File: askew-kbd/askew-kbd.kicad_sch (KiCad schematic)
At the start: 45 parts, among them SW1 SW_PUSH, SW10 SW_PUSH, SW11 SW_PUSH, SW12 SW_PUSH, SW13 SW_PUSH, SW14 SW_PUSH, SW15 SW_PUSH, SW16 SW_PUSH, SW17 SW_PUSH, SW18 SW_PUSH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

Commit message: unrouted base
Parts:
- U1: footprint kbd:ProMicro_v2 -> kbd:ProMicro_v3
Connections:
- net bottom: now also U1.11 (8/B4)
- net home: now also U1.10 (7/E6)
- net thumb: now also U1.12 (9/B5)
- net top: now also U1.9 (6/D7)
- net VCC: now reaches U1.21 (VCC)
- net reset: now reaches U1.22 (RST)
- net GND: now reaches U1.23 (GND)
- net GND: now also U1.3 (GND), U1.4 (GND)
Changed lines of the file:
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@@
   (junction (at 123.19 64.135) (diameter 0) (color 0 0 0 0)
   )
+  (junction (at 55.88 52.07) (diameter 0) (color 0 0 0 0)
+  )
   (junction (at 160.655 83.82) (diameter 0) (color 0 0 0 0)
   )
@@
     (stroke (width 0) (type default) (color 0 0 0 0))
   )
+  (wire (pts (xy 53.34 52.07) (xy 55.88 52.07))
+    (stroke (width 0) (type default) (color 0 0 0 0))
+  )
   (wire (pts (xy 123.19 52.07) (xy 123.19 64.135))
     (stroke (width 0) (type default) (color 0 0 0 0))
@@
     (stroke (width 0) (type default) (color 0 0 0 0))
   )
+  (wire (pts (xy 55.88 52.07) (xy 55.88 54.61))
+    (stroke (width 0) (type default) (color 0 0 0 0))
+  )
   (wire (pts (xy 203.2 83.82) (xy 225.425 83.82))
     (stroke (width 0) (type default) (color 0 0 0 0))
@@
   (wire (pts (xy 138.43 83.82) (xy 160.655 83.82))
     (stroke (width 0) (type default) (color 0 0 0 0))
+  )
+  (global_label "thumb" (shape input) (at 55.88 74.93 180) (fields_autoplaced)
+    (effects (font (size 1.27 1.27)) (justify right))
+    (property "Intersheet References" "${INTERSHEET_REFS}" (id 0) (at 47.6007 74.8506 0)
+      (effects (font (size 1.27 1.27)) (justify right) hide)
+    )
+  )
+  (global_label "bottom" (shape input) (at 55.88 72.39 180) (fields_autoplaced)
+    (effects (font (size 1.27 1.27)) (justify right))
+    (property "Intersheet References" "${INTERSHEET_REFS}" (id 0) (at 46.875 72.3106 0)
+      (effects (font (size 1.27 1.27)) (justify right) hide)
+    )
   )
   (global_label "col5" (shape input) (at 232.41 52.07 90) (fields_autoplaced)
@@
     )
   )
+  (global_label "reset" (shape input) (at 91.44 52.07 0) (fields_autoplaced)
+    (effects (font (size 1.27 1.27)) (justify left))
+    (property "Intersheet References" "${INTERSHEET_REFS}" (id 0) (at 98.5702 51.9906 0)
+      (effects (font (size 1.27 1.27)) (justify left) hide)
+    )
+  )
   (global_label "col0" (shape input) (at 123.19 52.07 90) (fields_autoplaced)
     (effects (font (size 1.27 1.27)) (justify left))
@@
     (property "Intersheet References" "${INTERSHEET_REFS}" (id 0) (at 166.2906 45.5445 90)
       (effects (font (size 1.27 1.27)) (justify left) hide)
+    )
+  )
+  (global_label "home" (shape input) (at 55.88 69.85 180) (fields_autoplaced)
+    (effects (font (size 1.27 1.27)) (justify right))
+    (property "Intersheet References" "${INTERSHEET_REFS}" (id 0) (at 48.3869 69.7706 0)
+      (effects (font (size 1.27 1.27)) (justify right) hide)
     )
   )
@@
     )
   )
+  (global_label "top" (shape input) (at 55.88 67.31 180) (fields_autoplaced)
+    (effects (font (size 1.27 1.27)) (justify right))
+    (property "Intersheet References" "${INTERSHEET_REFS}" (id 0) (at 50.4431 67.2306 0)
+      (effects (font (size 1.27 1.27)) (justify right) hide)
+    )
+  )
   (global_label "thumb" (shape input) (at 159.385 95.885 180) (fields_autoplaced)
     (effects (font (size 1.27 1.27)) (justify right))
@@
     (pin "2")
   )
+  (symbol (lib_id "power:GND") (at 53.34 52.07 270) (unit 1)
+    (in_bom yes) (on_board yes) (fields_autoplaced)
+    (property "Reference" "#PWR0103" (id 0) (at 46.99 52.07 0)
+      (effects (font (size 1.27 1.27)) hide)
+    )
+    (property "Value" "GND" (id 1) (at 49.53 52.0699 90)
+      (effects (font (size 1.27 1.27)) (justify right))
+    )
+    (property "Footprint" "" (id 2) (at 53.34 52.07 0)
+      (effects (font (size 1.27 1.27)) hide)
+    )
+    (property "Datasheet" "" (id 3) (at 53.34 52.07 0)
+      (effects (font (size 1.27 1.27)) hide)
+    )
+    (pin "1")
+  )
   (symbol (lib_id "kbd:SW_PUSH") (at 173.99 52.07 0) (unit 1)
     (in_bom yes) (on_board yes)
@@
     (pin "2")
   )
+  (symbol (lib_id "power:GND") (at 91.44 49.53 90) (unit 1)
+    (in_bom yes) (on_board yes) (fields_autoplaced)
+    (property "Reference" "#PWR0102" (id 0) (at 97.79 49.53 0)
+      (effects (font (size 1.27 1.27)) hide)
+    )
+    (property "Value" "GND" (id 1) (at 94.615 49.5299 90)
+      (effects (font (size 1.27 1.27)) (justify right))
+    )
+    (property "Footprint" "" (id 2) (at 91.44 49.53 0)
+      (effects (font (size 1.27 1.27)) hide)
+    )
+    (property "Datasheet" "" (id 3) (at 91.44 49.53 0)
+      (effects (font (size 1.27 1.27)) hide)
+    )
+    (pin "1")
+  )
   (symbol (lib_id "Simulation_SPICE:DIODE") (at 225.425 55.88 270) (unit 1)
     (in_bom yes) (on_board yes) (fields_autoplaced)
@@
       (effects (font (size 1.524 1.524)))
     )
-    (property "Footprint" "kbd:ProMicro_v2" (id 2) (at 76.2 87.63 0)
+    (property "Footprint" "kbd:ProMicro_v3" (id 2) (at 76.2 87.63 0)
       (effects (font (size 1.524 1.524)) hide)
     )
@@
     (pin "9")
   )
+  (symbol (lib_id "power:VCC") (at 91.44 54.61 270) (unit 1)
+    (in_bom yes) (on_board yes) (fields_autoplaced)
+    (property "Reference" "#PWR0101" (id 0) (at 87.63 54.61 0)
+      (effects (font (size 1.27 1.27)) hide)
+    )
+    (property "Value" "VCC" (id 1) (at 95.25 54.6099 90)
+      (effects (font (size 1.27 1.27)) (justify left))
+    )
+    (property "Footprint" "" (id 2) (at 91.44 54.61 0)
+      (effects (font (size 1.27 1.27)) hide)
+    )
+    (property "Datasheet" "" (id 3) (at 91.44 54.61 0)
+      (effects (font (size 1.27 1.27)) hide)
+    )
+    (pin "1")
+  )
   (symbol (lib_id "Simulation_SPICE:DIODE") (at 225.425 92.075 270) (unit 1)
     (in_bom yes) (on_board yes) (fields_autoplaced)
@@
   )
   (symbol_instances
+    (path "/f0639bb0-07b1-4aa0-9993-5be7eb782a33"
+      (reference "#PWR0101") (unit 1) (value "VCC") (footprint "")
+    )
+    (path "/a5e14191-2007-49d0-9d0e-26dfbbf2064d"
+      (reference "#PWR0102") (unit 1) (value "GND") (footprint "")
+    )
+    (path "/3364f424-941d-46ab-b111-d042aaac1a20"
+      (reference "#PWR0103") (unit 1) (value "GND") (footprint "")
+    )
     (path "/42c8422a-0c6f-45d3-bdef-b23e39cec6ea"
       (reference "D1") (unit 1) (value "DIODE") (footprint "kbd:D3_SMD")
@@
     )
     (path "/e8eb8608-eae3-4ab9-86a9-a5fe127a10fe"
-      (reference "U1") (unit 1) (value "ProMicro") (footprint "kbd:ProMicro_v2")
-    )
-  )
+      (reference "U1") (unit 1) (value "ProMicro") (footprint "kbd:ProMicro_v3")
+    )
+  )

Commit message: outline
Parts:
- added J1: OLED, kbd:OLED_v2, symbol Connector_Generic:Conn_01x04
- added J2: MJ-4PP-9, kbd:MJ-4PP-9, symbol corne-chocolate-rescue:MJ-4PP-9-kbd
- added JP1, JP2, JP3, JP4, JP5, JP6, JP7, JP8: (no value), kbd:Jumper, symbol corne-chocolate-rescue:Jumper_NO_Small-Device
- added JP9: (no value), kbd:JPC2, symbol corne-chocolate-rescue:Jumper-Device
- added RSW1: SW_PUSH, kbd:ResetSW, symbol corne-chocolate-rescue:SW_PUSH-kbd
- U1: footprint kbd:ProMicro_v3 -> keyboard_reversible:ProMicro_unrouted
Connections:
- net GND: now also J2.A, J2.B, JP1.1, JP8.1, RSW1.2
- net VCC: now also J2.D, JP2.1, JP7.1
- net reset: now also RSW1.1
- net data: now reaches U1.2 (RX1/D2)
- net data: now also JP9.1
- net SDA: now reaches U1.5 (2/D1/SDA)
- net SDA: now also JP4.1, JP5.1
- net SCL: now reaches U1.6 (3/D0/SCL)
- net SCL: now also JP3.1, JP6.1
- new net: J1.4 (Pin_4), JP1.2, JP5.2
- new net: J1.2 (Pin_2), JP3.2, JP7.2
- new net: J1.1 (Pin_1), JP4.2, JP8.2
- new net: J2.C, JP9.2
- new net: J1.3 (Pin_3), JP2.2, JP6.2

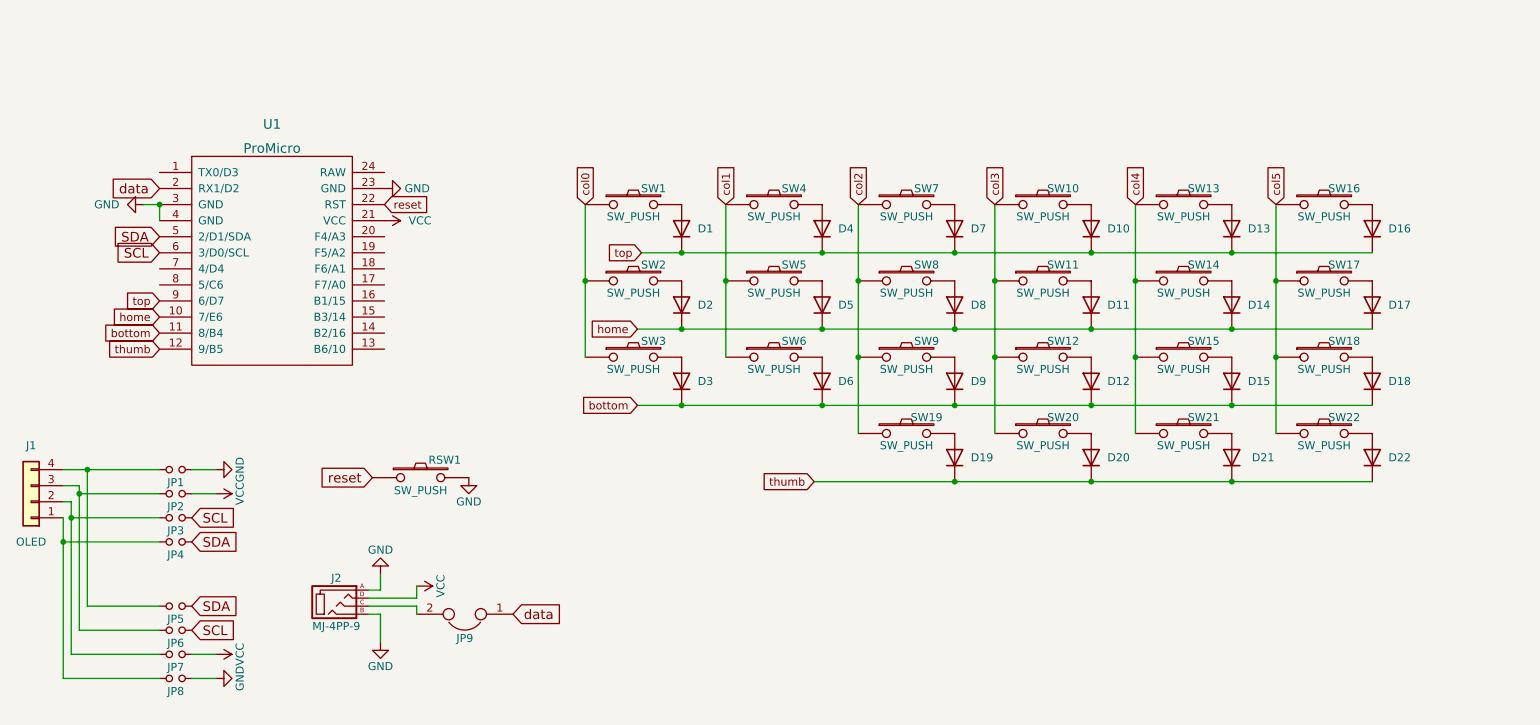
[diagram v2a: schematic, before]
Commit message: mounting holes
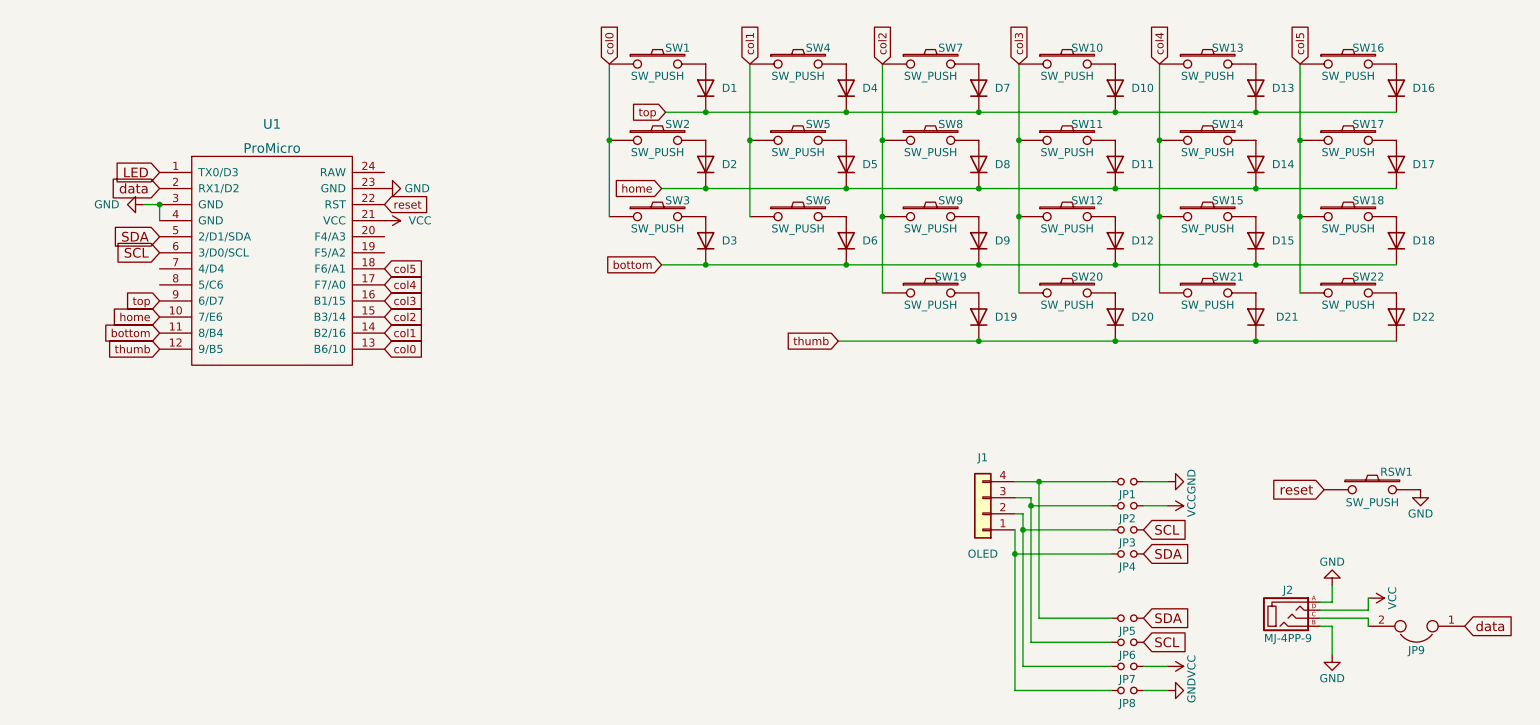
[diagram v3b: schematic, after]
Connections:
- net col0: now also U1.13 (B6/10)
- net col1: now also U1.14 (B2/16)
- net col2: now also U1.15 (B3/14)
- net col3: now also U1.16 (B1/15)
- net col4: now also U1.17 (F7/A0)
- net col5: now also U1.18 (F6/A1)
- net LED: now reaches U1.1 (TX0/D3)
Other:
- moved on the sheet: D1, D10, D11, D12, D13, D14, D15, D16, D17, D18, D19, D2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

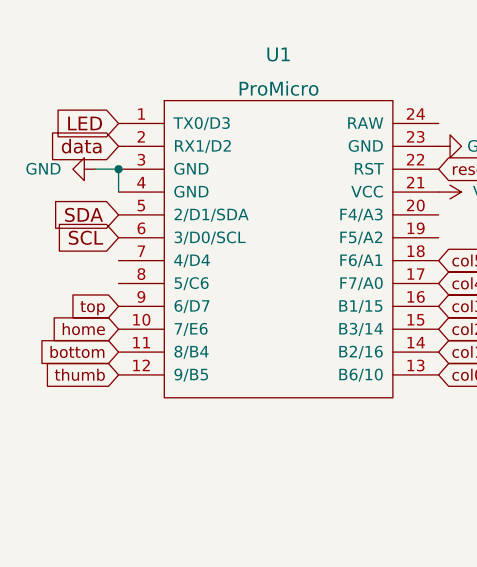
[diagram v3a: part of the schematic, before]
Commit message: remove buzzer and add diodes silk
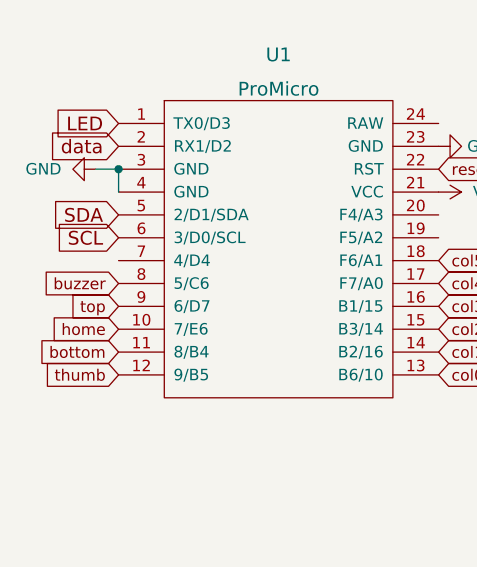
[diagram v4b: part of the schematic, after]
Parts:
- D1, D10, D11, D12, D13, D14, D15, D16, D17, D18, D19, D2, D20, D21, D22, D3, D4, D5, D6, D7, D8, D9: footprint kbd:D3_SMD -> fp:D3_SMD
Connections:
- net buzzer: now reaches U1.8 (5/C6)

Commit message: choc_spacing
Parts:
- SW1, SW10, SW11, SW12, SW13, SW14, SW15, SW16, SW17, SW18, SW2, SW21, SW3, SW4, SW5, SW6, SW7, SW8, SW9: footprint fp:ChocV1_V2_Hotswap_reversed -> fp:ChocV1_V2_Hotswap_reversed_choc_spacing
- SW19, SW20, SW22: footprint fp:ChocV1_V2_Hotswap_reversed_15u -> fp:ChocV1_V2_Hotswap_reversed_15u_choc_spacing

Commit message: redo layout
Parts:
- D1, D10, D11, D12, D13, D14, D15, D16, D17, D18, D19, D2, D20, D21, D22, D3, D4, D5, D6, D7, D8, D9: footprint fp:D3_SMD -> kbd:D3_TH_SMD

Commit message: basic routing
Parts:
- U1: footprint keyboard_reversible:ProMicro_unrouted -> fp:ProMicro_unrouted_type_c
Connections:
- net LED is gone; now on net col5: U1.1 (TX0/D3)
- net buzzer is gone; now on net col3: U1.8 (5/C6)
- net bottom: now also U1.18 (F6/A1); no longer U1.11 (8/B4)
- net col0: now also U1.11 (8/B4); no longer U1.13 (B6/10)
- net col1: now also U1.10 (7/E6); no longer U1.14 (B2/16)
- net col2: now also U1.9 (6/D7); no longer U1.15 (B3/14)
- net col3: no longer U1.16 (B1/15)
- net col4: now also U1.7 (4/D4); no longer U1.17 (F7/A0)
- net col5: no longer U1.18 (F6/A1)
- net home: now also U1.19 (F5/A2); no longer U1.10 (7/E6)
- net top: now also U1.20 (F4/A3); no longer U1.9 (6/D7)
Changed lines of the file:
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@@
     )
   )
-  (global_label "col0" (shape input) (at 91.44 74.93 0) (fields_autoplaced)
-    (effects (font (size 1.27 1.27)) (justify left))
-    (property "Intersheet References" "${INTERSHEET_REFS}" (id 0) (at 97.9655 74.8506 0)
-      (effects (font (size 1.27 1.27)) (justify left) hide)
+  (global_label "col0" (shape input) (at 55.88 72.39 180) (fields_autoplaced)
+    (effects (font (size 1.27 1.27)) (justify right))
+    (property "Intersheet References" "${INTERSHEET_REFS}" (id 0) (at 49.3545 72.4694 0)
+      (effects (font (size 1.27 1.27)) (justify right) hide)
     )
   )
@@
     )
   )
-  (global_label "bottom" (shape input) (at 55.88 72.39 180) (fields_autoplaced)
-    (effects (font (size 1.27 1.27)) (justify right))
-    (property "Intersheet References" "${INTERSHEET_REFS}" (id 0) (at 46.875 72.3106 0)
-      (effects (font (size 1.27 1.27)) (justify right) hide)
+  (global_label "bottom" (shape input) (at 91.44 62.23 0) (fields_autoplaced)
+    (effects (font (size 1.27 1.27)) (justify left))
+    (property "Intersheet References" "${INTERSHEET_REFS}" (id 0) (at 100.445 62.3094 0)
+      (effects (font (size 1.27 1.27)) (justify left) hide)
     )
   )
@@
     )
   )
-  (global_label "col5" (shape input) (at 91.44 62.23 0) (fields_autoplaced)
-    (effects (font (size 1.27 1.27)) (justify left))
-    (property "Intersheet References" "${INTERSHEET_REFS}" (id 0) (at 97.9655 62.1506 0)
-      (effects (font (size 1.27 1.27)) (justify left) hide)
+  (global_label "col5" (shape input) (at 55.88 46.99 180) (fields_autoplaced)
+    (effects (font (size 1.27 1.27)) (justify right))
+    (property "Intersheet References" "${INTERSHEET_REFS}" (id 0) (at 49.3545 47.0694 0)
+      (effects (font (size 1.27 1.27)) (justify right) hide)
     )
   )
@@
     )
   )
-  (global_label "LED" (shape input) (at 55.88 46.99 180) (fields_autoplaced)
-    (effects (font (size 1.524 1.524)) (justify right))
-    (property "Intersheet References" "${INTERSHEET_REFS}" (id 0) (at 264.795 142.875 0)
-      (effects (font (size 1.27 1.27)) hide)
-    )
-  )
-  (global_label "col3" (shape input) (at 91.44 67.31 0) (fields_autoplaced)
-    (effects (font (size 1.27 1.27)) (justify left))
-    (property "Intersheet References" "${INTERSHEET_REFS}" (id 0) (at 97.9655 67.2306 0)
-      (effects (font (size 1.27 1.27)) (justify left) hide)
+  (global_label "col3" (shape input) (at 55.88 64.77 180) (fields_autoplaced)
+    (effects (font (size 1.27 1.27)) (justify right))
+    (property "Intersheet References" "${INTERSHEET_REFS}" (id 0) (at 49.3545 64.8494 0)
+      (effects (font (size 1.27 1.27)) (justify right) hide)
     )
   )
@@
     )
   )
-  (global_label "col1" (shape input) (at 91.44 72.39 0) (fields_autoplaced)
-    (effects (font (size 1.27 1.27)) (justify left))
-    (property "Intersheet References" "${INTERSHEET_REFS}" (id 0) (at 97.9655 72.3106 0)
-      (effects (font (size 1.27 1.27)) (justify left) hide)
-    )
-  )
-  (global_label "buzzer" (shape input) (at 55.88 64.77 180) (fields_autoplaced)
+  (global_label "col1" (shape input) (at 55.88 69.85 180) (fields_autoplaced)
     (effects (font (size 1.27 1.27)) (justify right))
-    (property "Intersheet References" "${INTERSHEET_REFS}" (id 0) (at 47.2379 64.6906 0)
+    (property "Intersheet References" "${INTERSHEET_REFS}" (id 0) (at 49.3545 69.9294 0)
       (effects (font (size 1.27 1.27)) (justify right) hide)
     )
@@
     )
   )
-  (global_label "col2" (shape input) (at 91.44 69.85 0) (fields_autoplaced)
+  (global_label "col2" (shape input) (at 55.88 67.31 180) (fields_autoplaced)
+    (effects (font (size 1.27 1.27)) (justify right))
+    (property "Intersheet References" "${INTERSHEET_REFS}" (id 0) (at 49.3545 67.3894 0)
+      (effects (font (size 1.27 1.27)) (justify right) hide)
+    )
+  )
+  (global_label "home" (shape input) (at 91.44 59.69 0) (fields_autoplaced)
     (effects (font (size 1.27 1.27)) (justify left))
-    (property "Intersheet References" "${INTERSHEET_REFS}" (id 0) (at 97.9655 69.7706 0)
-      (effects (font (size 1.27 1.27)) (justify left) hide)
-    )
-  )
-  (global_label "home" (shape input) (at 55.88 69.85 180) (fields_autoplaced)
-    (effects (font (size 1.27 1.27)) (justify right))
-    (property "Intersheet References" "${INTERSHEET_REFS}" (id 0) (at 48.3869 69.7706 0)
-      (effects (font (size 1.27 1.27)) (justify right) hide)
+    (property "Intersheet References" "${INTERSHEET_REFS}" (id 0) (at 98.9331 59.7694 0)
+      (effects (font (size 1.27 1.27)) (justify left) hide)
     )
   )
@@
     )
   )
-  (global_label "top" (shape input) (at 55.88 67.31 180) (fields_autoplaced)
+  (global_label "top" (shape input) (at 91.44 57.15 0) (fields_autoplaced)
+    (effects (font (size 1.27 1.27)) (justify left))
+    (property "Intersheet References" "${INTERSHEET_REFS}" (id 0) (at 96.8769 57.2294 0)
+      (effects (font (size 1.27 1.27)) (justify left) hide)
+    )
+  )
+  (global_label "col4" (shape input) (at 55.88 62.23 180) (fields_autoplaced)
     (effects (font (size 1.27 1.27)) (justify right))
-    (property "Intersheet References" "${INTERSHEET_REFS}" (id 0) (at 50.4431 67.2306 0)
+    (property "Intersheet References" "${INTERSHEET_REFS}" (id 0) (at 49.3545 62.3094 0)
       (effects (font (size 1.27 1.27)) (justify right) hide)
-    )
-  )
-  (global_label "col4" (shape input) (at 91.44 64.77 0) (fields_autoplaced)
-    (effects (font (size 1.27 1.27)) (justify left))
-    (property "Intersheet References" "${INTERSHEET_REFS}" (id 0) (at 97.9655 64.6906 0)
-      (effects (font (size 1.27 1.27)) (justify left) hide)
     )
   )
@@
       (effects (font (size 1.524 1.524)))
     )
-    (property "Footprint" "keyboard_reversible:ProMicro_unrouted" (id 2) (at 76.2 87.63 0)
+    (property "Footprint" "fp:ProMicro_unrouted_type_c" (id 2) (at 76.2 87.63 0)
       (effects (font (size 1.524 1.524)) hide)
     )
@@
     )
     (path "/e8eb8608-eae3-4ab9-86a9-a5fe127a10fe"
-      (reference "U1") (unit 1) (value "ProMicro") (footprint "keyboard_reversible:ProMicro_unrouted")
-    )
-  )
+      (reference "U1") (unit 1) (value "ProMicro") (footprint "fp:ProMicro_unrouted_type_c")
+    )
+  )

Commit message: routing
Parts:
- removed JP9: (no value), kbd:JPC2, symbol corne-chocolate-rescue:Jumper-Device
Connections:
- net data: now also J2.C
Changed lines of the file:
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@@
     )
   )
-  (global_label "data" (shape input) (at 262.255 118.745 0) (fields_autoplaced)
+  (global_label "data" (shape input) (at 247.015 118.745 0) (fields_autoplaced)
     (effects (font (size 1.524 1.524)) (justify left))
-    (property "Intersheet References" "${INTERSHEET_REFS}" (id 0) (at 163.195 33.02 0)
+    (property "Intersheet References" "${INTERSHEET_REFS}" (id 0) (at 147.955 33.02 0)
       (effects (font (size 1.27 1.27)) hide)
     )
@@
     (property "Spice_Primitive" "D" (id 5) (at 185.42 45.72 0)
       (effects (font (size 1.27 1.27)) (justify left) hide)
-    )
-    (pin "1")
-    (pin "2")
-  )
-  (symbol (lib_id "corne-chocolate-rescue:Jumper-Device") (at 254.635 118.745 180) (unit 1)
-    (in_bom yes) (on_board yes)
-    (property "Reference" "JP9" (id 0) (at 254.635 122.555 0))
-    (property "Value" " " (id 1) (at 254.635 116.713 0))
-    (property "Footprint" "kbd:JPC2" (id 2) (at 254.635 118.745 0)
-      (effects (font (size 1.27 1.27)) hide)
-    )
-    (property "Datasheet" "" (id 3) (at 254.635 118.745 0)
-      (effects (font (size 1.27 1.27)) hide)
     )
     (pin "1")
@@
       (reference "JP8") (unit 1) (value " ") (footprint "kbd:Jumper")
     )
-    (path "/da23330d-fc11-4bf8-959a-f59ce3c5ac2f"
-      (reference "JP9") (unit 1) (value " ") (footprint "kbd:JPC2")
-    )
     (path "/9d6d523b-97e2-4003-8ae7-75f1f7945278"
